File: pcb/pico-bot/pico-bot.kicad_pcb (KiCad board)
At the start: 2 copper layers, 101.6 x 54.6 mm, 62 parts, among them J1 Conn_01x02_Male, J2 Conn_01x06_Male, J3 Conn_01x06_Male, J4 Conn_01x06_Male, J5 Conn_01x06_Male, Q1 DMG2305UX, Q2 AOD417, SW1 SW_SPDT, SW2 SW_Push, SW3 SW_Push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

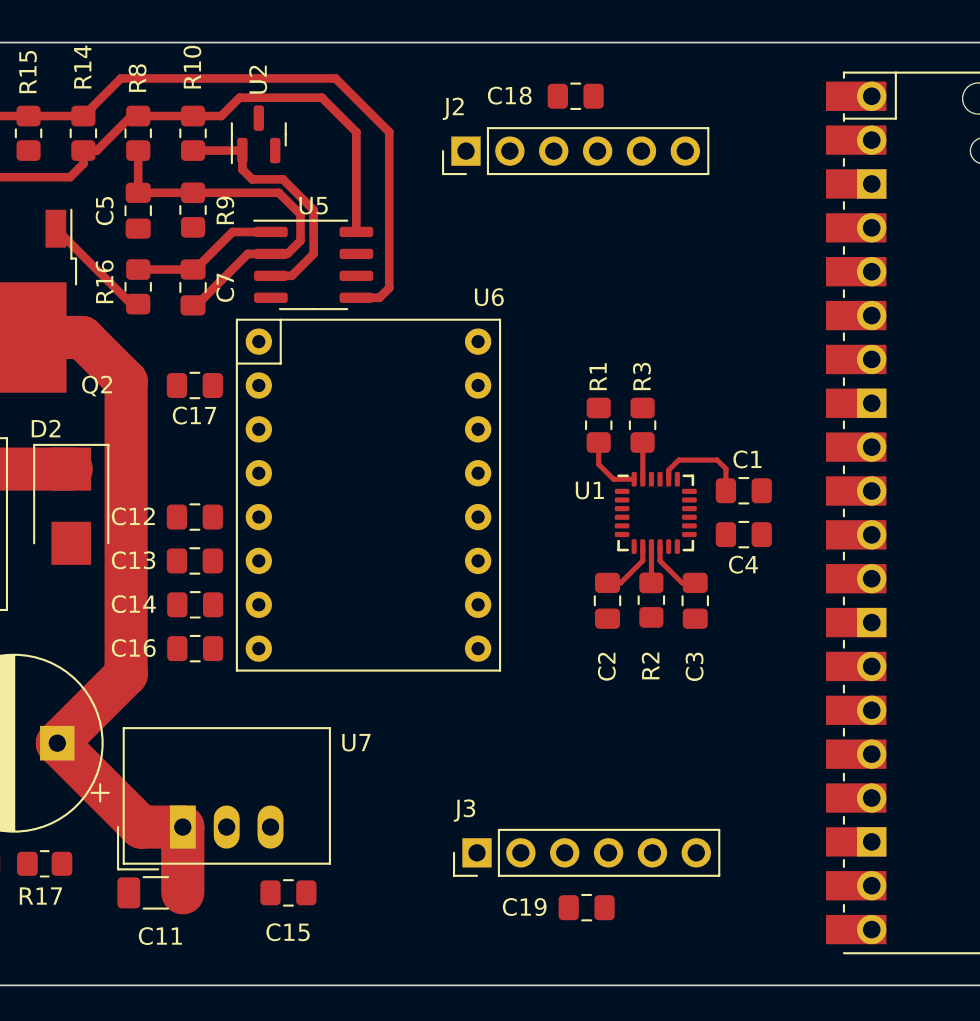
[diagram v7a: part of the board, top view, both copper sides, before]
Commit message: Rework pin allocation to ease layout
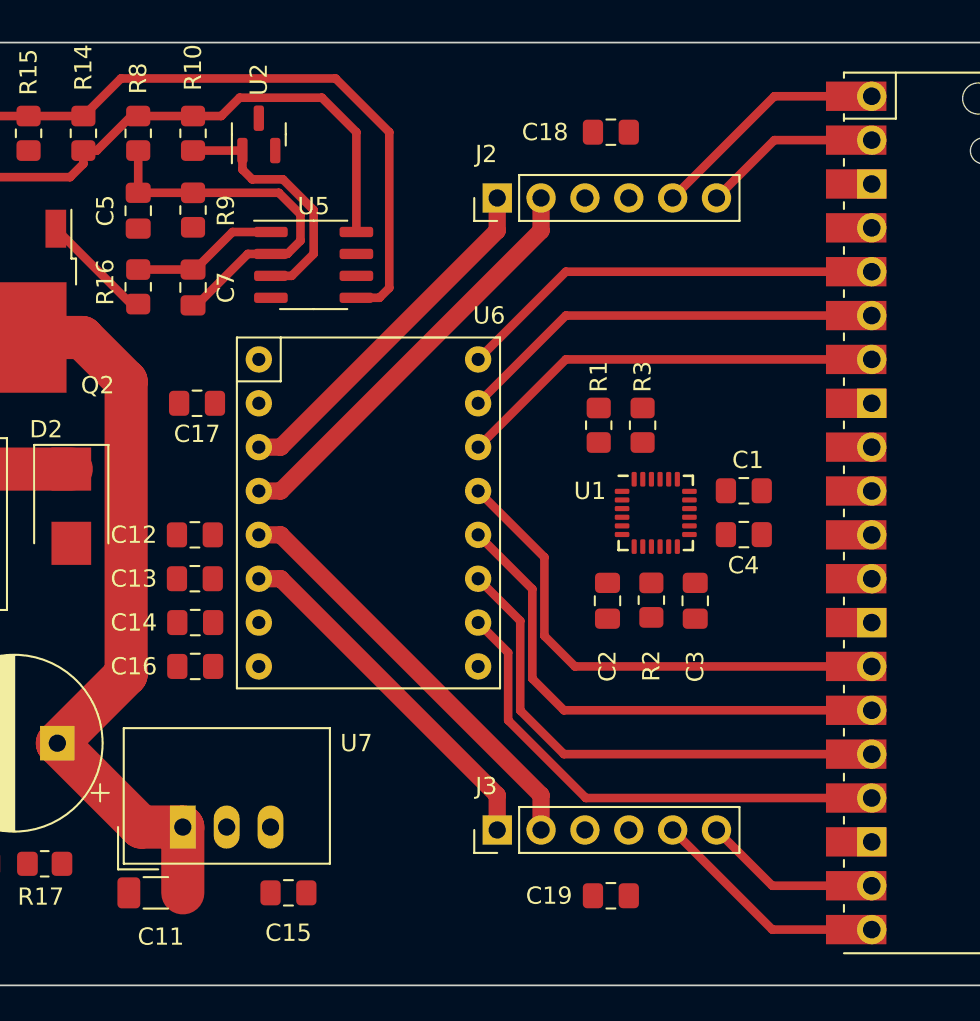
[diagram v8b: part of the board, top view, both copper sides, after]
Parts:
- moved J2 3.26 mm to (138.9, 75.5)
- moved C18 2.91 mm to (145.5, 71.7)
- moved J3 1.77 mm to (138.9, 112.1)
- moved C19 1.56 mm to (145.5, 115.9)
- moved C17 1.04 mm to (121.5, 87.4)
- moved C12 1.03 mm to (121.4, 95.0)
- moved C13 1.03 mm to (121.4, 97.5)
- moved C14 1.03 mm to (121.4, 100.1)
- moved C16 1.03 mm to (121.4, 102.6)
- moved U6 1.03 mm to (125.1, 84.8)
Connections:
- J4 pad 1: /GPIO0 -> /SPARE0
- J4 pad 2: /GPIO1 -> /SPARE1
- J4 pad 3: /GPIO9 -> /SPARE2
- J4 pad 4: /GPIO10 -> /SPARE3
- J4 pad 5: /GPIO27 -> /SPARE4
- J4 pad 6: /GPIO28 -> /SPARE5
- U4 pad 1: /GPIO0 -> /AENC1
- U4 pad 12: /GPIO9 -> /SPARE0
- U4 pad 14: /GPIO10 -> /STDBY
- U4 pad 15: /MODE -> /BIN1
- U4 pad 16: /AENC1 -> /BIN2
- U4 pad 17: /AENC2 -> /PWMB
- U4 pad 19: /BENC1 -> /BENC2
- U4 pad 2: /GPIO1 -> /AENC2
- U4 pad 20: /BENC2 -> /BENC1
- U4 pad 21: /PWMB -> /SPARE5
- U4 pad 22: /PWMA -> /SPARE4
- U4 pad 24: /BIN2 -> /SPARE3
- U4 pad 25: /BIN1 -> /SPARE2
- U4 pad 26: /AIN2 -> Net-(U4-Pad26)
- U4 pad 27: /AIN1 -> Net-(U4-Pad27)
- U4 pad 29: /STDBY -> Net-(U4-Pad29)
- U4 pad 32: /GPIO27 -> /SPARE1
- U4 pad 34: /GPIO28 -> /MODE
- U4 pad 5: Net-(R4-Pad2) -> /PWMA
- U4 pad 6: Net-(R5-Pad2) -> /AIN2
- U4 pad 7: Net-(R6-Pad2) -> /AIN1
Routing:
- net /BIN2: track 0.00 -> 30.0 mm
- net /BIN1: track 0.00 -> 30.0 mm
- net /STDBY: track 0.00 -> 29.7 mm
- net /PWMB: track 0.00 -> 29.3 mm
- net /AIN1: track 0.00 -> 24.9 mm
- net /PWMA: track 0.00 -> 24.9 mm
- net /AIN2: track 0.00 -> 24.9 mm
- net /BOUT2: track 0.00 -> 24.6 mm
- net /AOUT2: track 0.00 -> 24.5 mm
- net /BOUT1: track 0.00 -> 21.0 mm
- net /AOUT1: track 0.00 -> 20.9 mm
- net /AENC1: track 0.00 -> 14.0 mm
- net /BENC1: track 0.00 -> 13.9 mm
- net /AENC2: track 0.00 -> 10.4 mm
- net /BENC2: track 0.00 -> 10.3 mm
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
